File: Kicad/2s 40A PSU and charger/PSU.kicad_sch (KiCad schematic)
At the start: 72 parts, among them J5 JST XH-S, Q1 PJA3430, Q2 PJA3430, Q3 Vishay sir404dp, Q4 PJA3430, Q5 PJA3430, Q7 Vishay sir404dp, U2 AP63203WU, U3 BQ76905RGRR, U4 BQ24780SRUYR

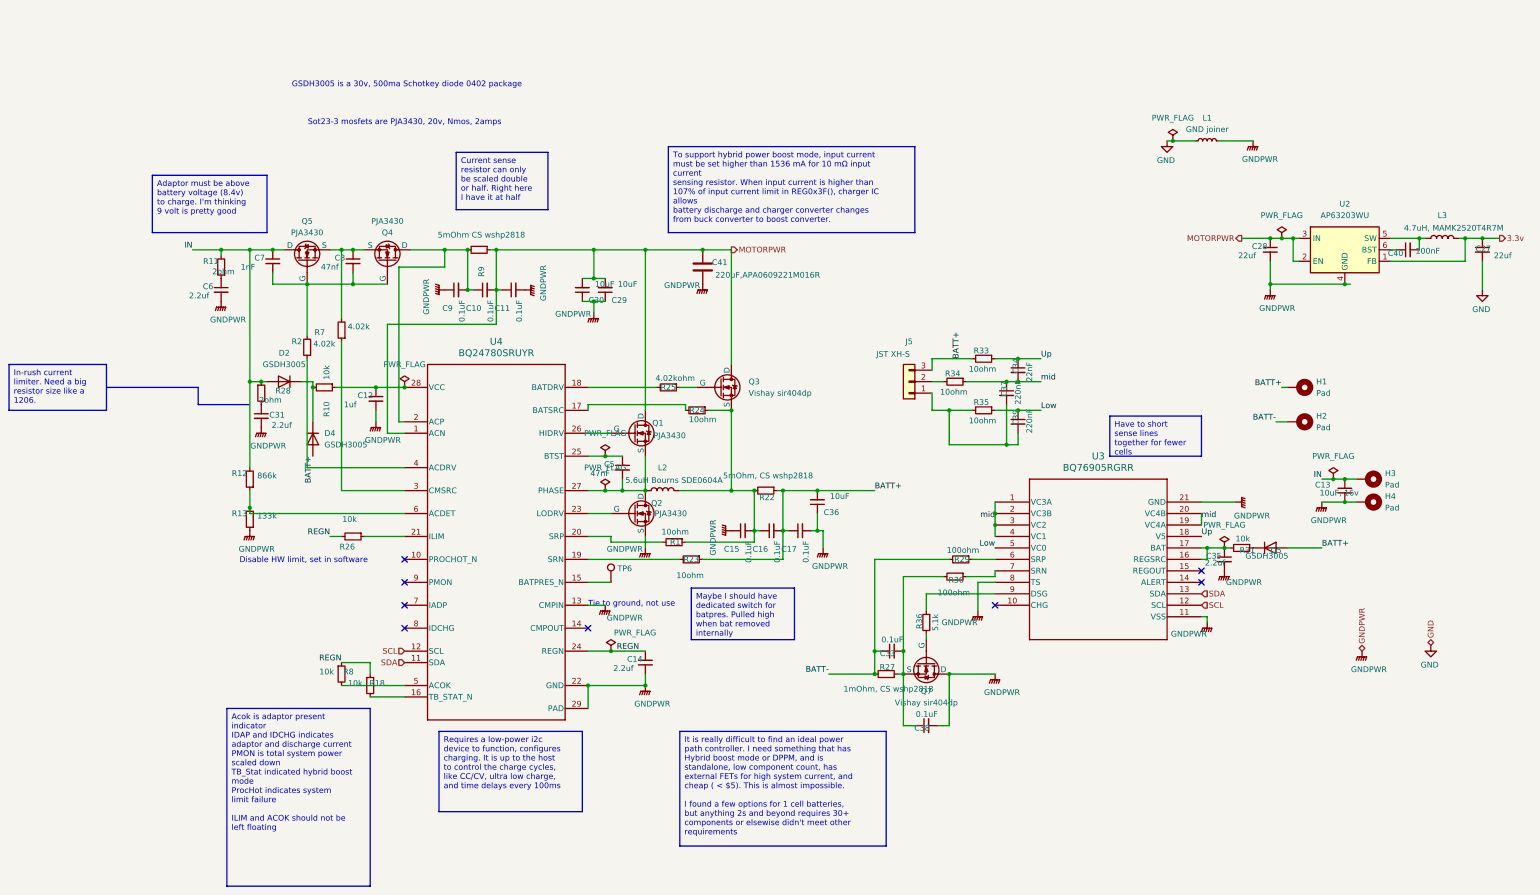
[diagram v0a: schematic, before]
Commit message: Rearranged schematic hierarchy
It should be clearer than the original design from my testing board. I haven't changed any of the design things except getting the correct small transistor footprint (errata from before)
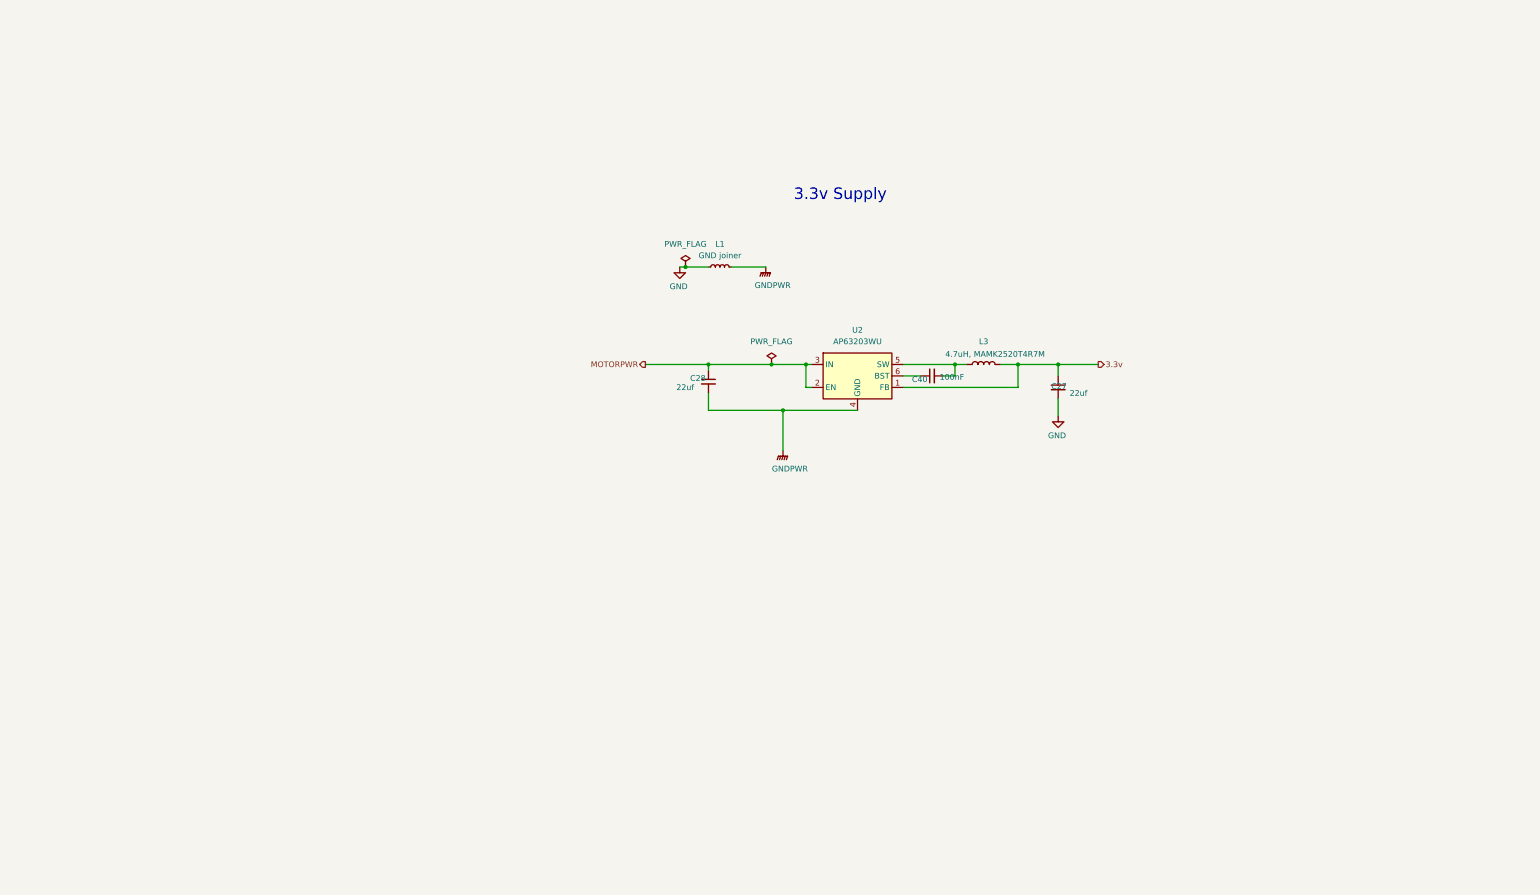
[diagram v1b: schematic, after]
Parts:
- removed C10, C11, C15, C16, C17, C33, C38, C9: 0.1uF, Capacitor_SMD:C_0603_1608Metric, symbol Device:C_Small
- removed C12: 1uf, Capacitor_SMD:C_0603_1608Metric, symbol Device:C_Small
- removed C13: 10uF, 16v, Capacitor_SMD:C_0603_1608Metric_Pad1.08x0.95mm_HandSolder, symbol Device:C_Small
- removed C14, C31, C35, C6: 2.2uf, Capacitor_SMD:C_0603_1608Metric, symbol Device:C_Small
- removed C29, C30, C36: 10uF, Capacitor_SMD:C_0603_1608Metric, symbol Device:C_Small
- removed C34: 22nF, Capacitor_SMD:C_0603_1608Metric, symbol Device:C_Small
- removed C37, C39: 220nF, Capacitor_SMD:C_0603_1608Metric, symbol Device:C_Small
- removed C41: 220uF,APA0609221M016R, Capacitor_SMD:CP_Elec_6.3x9.9, symbol Device:C
- removed C5: 47nF, Capacitor_SMD:C_0603_1608Metric, symbol Device:C_Small
- removed C7: 1nF, Capacitor_SMD:C_0603_1608Metric, symbol Device:C_Small
- removed C8: 47nf, Capacitor_SMD:C_0603_1608Metric, symbol Device:C_Small
- removed D2, D4, D5: GSDH3005, Diode_SMD:D_0402_1005Metric, symbol Device:D
- removed H1, H2, H3, H4: Pad, TestPoint:TestPoint_Pad_3.0x3.0mm, symbol Mechanical:MountingHole_Pad
- removed J5: JST XH-S, Connector_JST:JST_XH_S3B-XH-A_1x03_P2.50mm_Horizontal, symbol Connector_Generic:Conn_01x03
- removed L2: 5.6uH Bourns SDE0604A, Inductor_SMD:L_Bourns_SDR0604, symbol Device:L
- removed Q1, Q2, Q4, Q5: PJA3430, Package_TO_SOT_SMD:SOT-323_SC-70, symbol Simulation_SPICE:NMOS
- removed Q3, Q7: Vishay sir404dp, Package_DFN_QFN:PQFN-8-EP_6x5mm_P1.27mm_Generic, symbol Simulation_SPICE:NMOS
- removed R1, R23, R24, R33, R34, R35: 10ohm, Resistor_SMD:R_0603_1608Metric, symbol Device:R_Small
- removed R10, R18, R26, R31, R8: 10k, Resistor_SMD:R_0603_1608Metric, symbol Device:R_Small
- removed R11, R28: 2ohm, Resistor_SMD:R_0603_1608Metric, symbol Device:R_Small
- removed R12: 866k, Resistor_SMD:R_0603_1608Metric, symbol Device:R_Small
- removed R13: 133k, Resistor_SMD:R_0603_1608Metric, symbol Device:R_Small
- removed R2, R7: 4.02k, Resistor_SMD:R_0603_1608Metric, symbol Device:R_Small
- removed R22: 5mOhm, CS wshp2818, Resistor_SMD:R_2816_7142Metric, symbol Device:R_Small
- removed R25: 4.02kohm, Resistor_SMD:R_0603_1608Metric, symbol Device:R_Small
- removed R27: 1mOhm, CS wshp2818, Resistor_SMD:R_2816_7142Metric, symbol Device:R_Small
- removed R29, R30: 100ohm, Resistor_SMD:R_0603_1608Metric, symbol Device:R_Small
- removed R36: 5.1k, Resistor_SMD:R_0603_1608Metric, symbol Device:R_Small
- removed R9: 5mOhm CS wshp2818, Resistor_SMD:R_2816_7142Metric, symbol Device:R_Small
- removed TP6: ~, TestPoint:TestPoint_Pad_D1.0mm, symbol Connector:TestPoint
- removed U3: BQ76905RGRR, BQ76905:VQFN20_RGR_TEX, symbol BQ76905:BQ76905RGRR
- removed U4: BQ24780SRUYR, BQ24780:RUY0028A, symbol BQ24780s:BQ24780SRUYR
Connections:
- no-connect marks 8 -> 0
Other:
- note added: "3.3v Supply"
- note removed: "Disable HW limit, set in software"
- note removed: "GSDH3005 is a 30v, 500ma Schotkey diode 0402 package"
- note removed: "Sot23-3 mosfets are PJA3430, 20v, Nmos, 2amps"
- note removed: "Tie to ground, not use"
- moved on the sheet: C27, C28, C40, L1, L3, U2

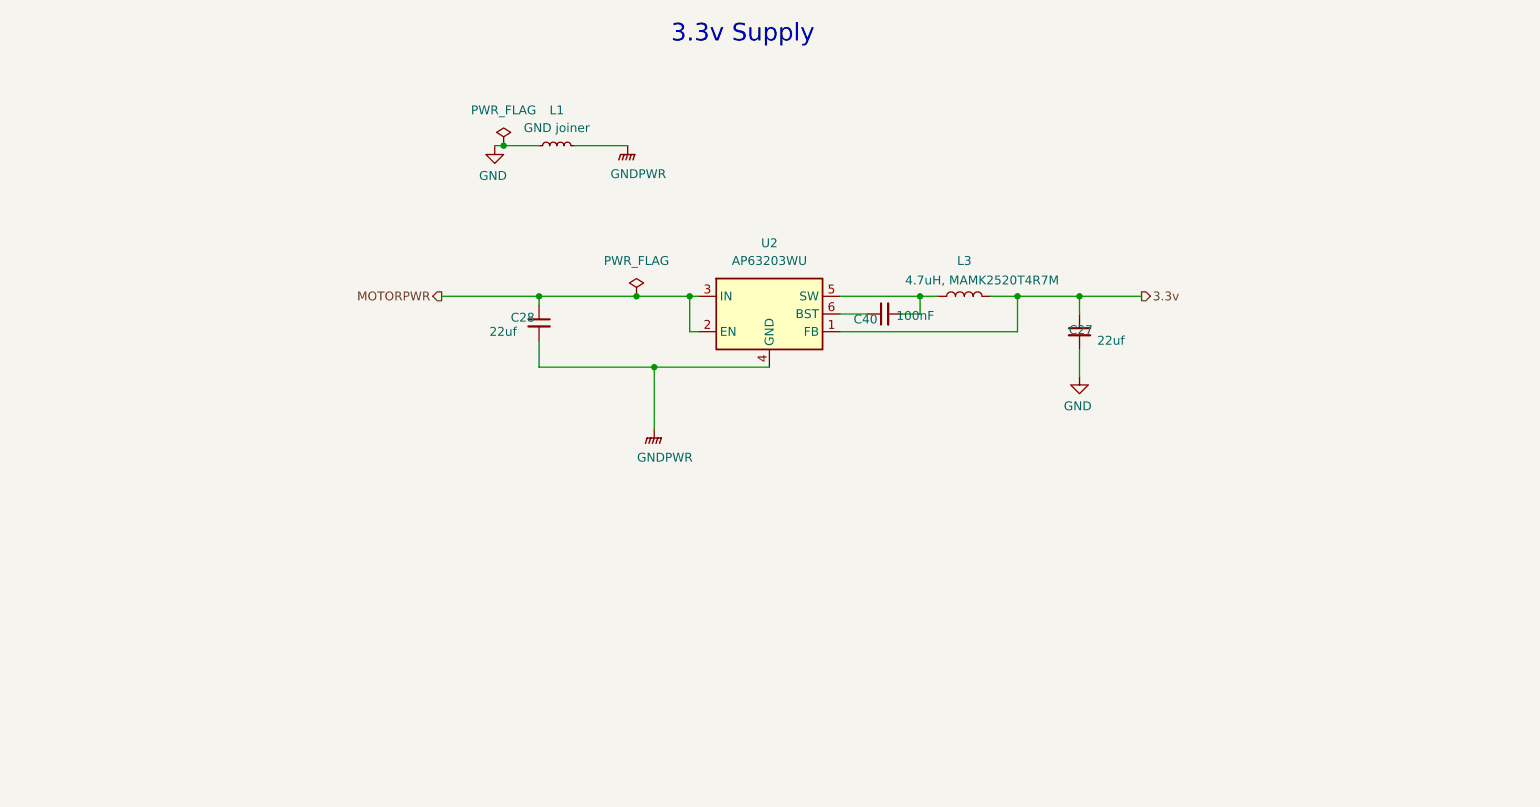
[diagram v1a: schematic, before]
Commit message: Reworked PSU to use CH32X035 and USB-PD
This will save a few bucks and will actually be a cooler solution than just a DC jack connected to some pads
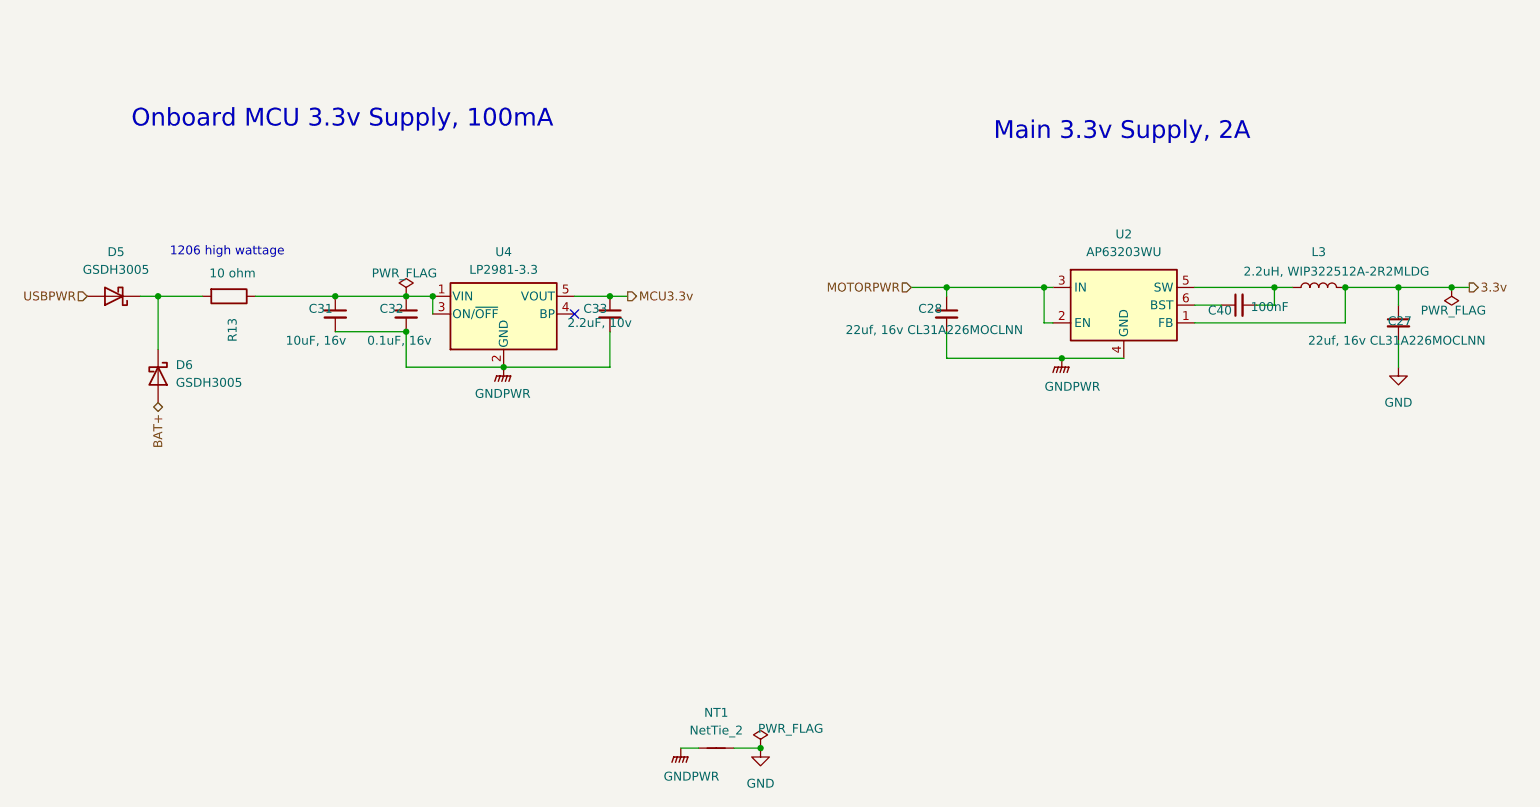
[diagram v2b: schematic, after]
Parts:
- removed L1: GND joiner, Jumper:SolderJumper-2_P1.3mm_Bridged_Pad1.0x1.5mm, symbol Device:L_Small
- added C31: 10uF, 16v, Capacitor_SMD:C_0603_1608Metric, symbol Device:C_Small
- added C32: 0.1uF, 16v, Capacitor_SMD:C_0402_1005Metric, symbol Device:C_Small
- added C33: 2.2uF, 10v, Capacitor_SMD:C_0402_1005Metric, symbol Device:C_Small
- added D5, D6: GSDH3005, Diode_SMD:D_0402_1005Metric, symbol Device:D_Schottky
- added NT1: NetTie_2, NetTie:NetTie-2_SMD_Pad0.5mm, symbol Device:NetTie_2
- added R13: 10 ohm, Resistor_SMD:R_0805_2012Metric, symbol Device:R
- added U4: LP2981-3.3, Package_TO_SOT_SMD:SOT-23-5, symbol Regulator_Linear:LP2985-3.3
- C27, C28: value 22uf -> 22uf, 16v CL31A226MOCLNN; footprint Capacitor_SMD:C_0603_1608Metric -> Capacitor_SMD:C_1206_3216Metric
- L3: value 4.7uH, MAMK2520T4R7M -> 2.2uH, WIP322512A-2R2MLDG
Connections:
- net GND: now also NT1.2
- net GNDPWR: now also C31.2, C32.2, C33.2, NT1.1, U4.2 (GND)
- new net: C31.1, C32.1, R13.1, U4.1 (VIN), U4.3 (ON/~{OFF})
- new net: D5.1 (K), D6.1 (K), R13.2
- new net BAT+: D6.2 (A)
- new net MCU3.3v: C33.1, U4.5 (VOUT)
- new net USBPWR: D5.2 (A)
- no-connect marks 0 -> 1
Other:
- note added: "1206 high wattage"
- note added: "Main 3.3v Supply, 2A"
- note added: "Onboard MCU 3.3v Supply, 100mA"
- note removed: "3.3v Supply"
- moved on the sheet: C27, C28, C40, L3, U2

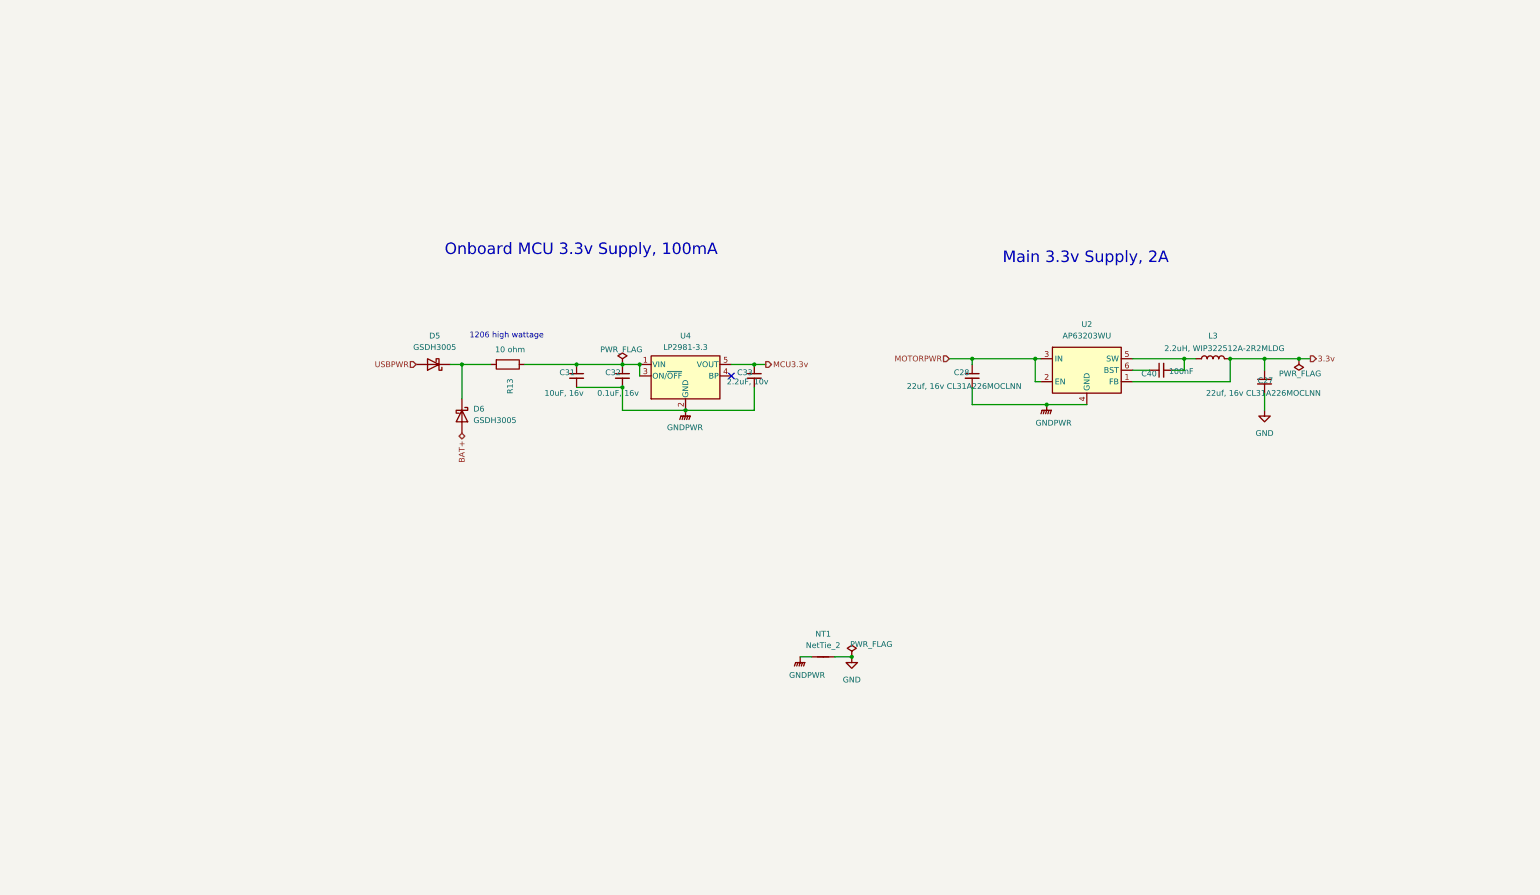
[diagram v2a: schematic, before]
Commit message: Improved schematic formatting and visuals
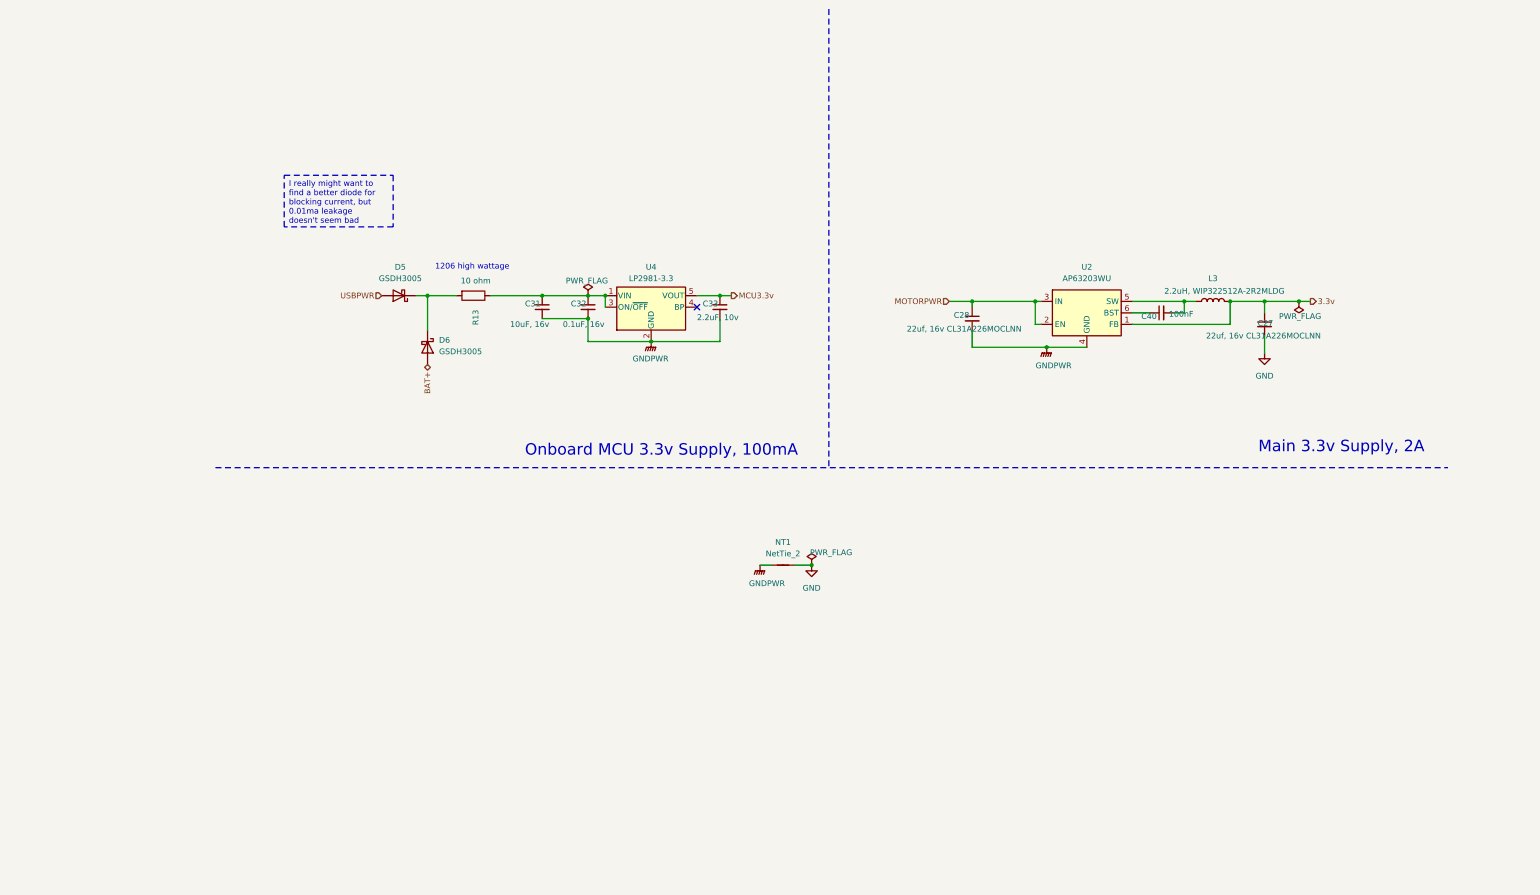
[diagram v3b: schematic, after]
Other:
- moved on the sheet: C27, C28, C31, C32, C33, C40, D5, D6, L3, NT1, R13, U2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
